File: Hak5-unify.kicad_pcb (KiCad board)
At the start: 2 copper layers, 26 x 17.5 mm, 4 parts, among them J1 Conn_01x04, J2 Conn_01x03, U1 Unify-Nano

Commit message: v0.1.1
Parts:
- removed 10K: R, Resistors_ThroughHole:R_Axial_DIN0204_L3.6mm_D1.6mm_P7.62mm_Horizontal
- added R1: R, Resistors_ThroughHole:R_Axial_DIN0204_L3.6mm_D1.6mm_P7.62mm_Horizontal, F.Cu at (104.0, 86.5)
- moved J1 1.00 mm to (123.2, 93.6)
- moved U1 0.63 mm to (106.1, 97.8)
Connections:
- J2 pad 1: Net-(J2-Pad1) -> +5V
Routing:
- net TX: track 35.3 -> 36.8 mm
- net +5V: track 5.03 -> 4.47 mm
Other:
- outline, holes or cut-outs redrawn
- board text added: "Cut Out"
- board text added: "v0.1.1"
- board text removed: "v0.1.0"

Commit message: v0.2.0
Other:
- outline, holes or cut-outs redrawn
- board text added: "v0.2.0"
- board text removed: "v0.1.1"
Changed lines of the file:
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@@
   (general
     (thickness 1.6)
-    (drawings 19)
+    (drawings 23)
     (tracks 17)
     (zones 0)
@@
     (uvia_drill 0.1)
   )
+  (module unify-nano:unify-nano (layer F.Cu)
+    (at 106.1 97.75)
+    (fp_text reference U1 (at 0.3 3.5) (layer F.SilkS)
+      (effects (font (size 1 1) (thickness 0.15)))
+    )
+    (fp_text value Unify-Nano (at 7 1) (layer F.Fab)
+      (effects (font (size 1 1) (thickness 0.15)))
+    )
+    (fp_line (start 0 0) (end 0 -13.1) (layer F.Fab) (width 0.15))
+    (fp_line (start 14.6 -13.1) (end 0 -13.1) (layer F.Fab) (width 0.15))
+    (fp_line (start 14.6 0) (end 14.6 -13.1) (layer F.Fab) (width 0.15))
+    (fp_line (start 0 0) (end 14.6 0) (layer F.Fab) (width 0.15))
+    (pad 9 thru_hole circle (at 12.2 -13.3) (size 1.524 1.524) (drill 0.762) (layers *.Cu *.Mask)
+      (net 9 "Net-(SW1-Pad2)"))
+    (pad 10 thru_hole circle (at 8.6 -13.3) (size 1.524 1.524) (drill 0.762) (layers *.Cu *.Mask)
+      (net 10 "Net-(SW1-Pad1)"))
+    (pad 8 thru_hole circle (at 14.8 -5) (size 1.524 1.524) (drill 0.762) (layers *.Cu *.Mask)
+      (net 11 "Net-(U1-Pad8)"))
+    (pad 7 thru_hole circle (at 14.7 -1.8) (size 1.524 1.524) (drill 0.762) (layers *.Cu *.Mask)
+      (net 12 "Net-(U1-Pad7)"))
+    (pad 6 thru_hole circle (at -0.25 -1.5) (size 1.524 1.524) (drill 0.762) (layers *.Cu *.Mask)
+      (net 2 +5V))
+    (pad 5 thru_hole circle (at -0.25 -3.5) (size 1.524 1.524) (drill 0.762) (layers *.Cu *.Mask)
+      (net 1 GND))
+    (pad 4 thru_hole circle (at -0.25 -5.5) (size 1.524 1.524) (drill 0.762) (layers *.Cu *.Mask)
+      (net 4 "Net-(U1-Pad4)"))
+    (pad 3 thru_hole circle (at -0.25 -7.5) (size 1.524 1.524) (drill 0.762) (layers *.Cu *.Mask)
+      (net 3 "Net-(U1-Pad3)"))
+    (pad 2 thru_hole circle (at -0.25 -9.5) (size 1.524 1.524) (drill 0.762) (layers *.Cu *.Mask)
+      (net 13 "Net-(J2-Pad3)"))
+    (pad 1 thru_hole circle (at -0.25 -11.5) (size 1.524 1.524) (drill 0.762) (layers *.Cu *.Mask)
+      (net 6 TX))
+  )
   (module Pin_Headers:Pin_Header_Straight_1x03_Pitch2.54mm (layer F.Cu)
     (at 101.6 96.2 180)
@@
       (rotate (xyz 0 0 0))
     )
-  )
-  (module unify-nano:unify-nano (layer F.Cu)
-    (at 106.1 97.8)
-    (fp_text reference U1 (at 0.3 3.5) (layer F.SilkS)
-      (effects (font (size 1 1) (thickness 0.15)))
-    )
-    (fp_text value Unify-Nano (at 7 1) (layer F.Fab)
-      (effects (font (size 1 1) (thickness 0.15)))
-    )
-    (fp_line (start 0 0) (end 0 -13.2) (layer F.Fab) (width 0.15))
-    (fp_line (start 14.65 -13.2) (end -0.05 -13.2) (layer F.Fab) (width 0.15))
-    (fp_line (start 14.65 0) (end 14.65 -13.2) (layer F.Fab) (width 0.15))
-    (fp_line (start 0.05 0) (end 14.65 0) (layer F.Fab) (width 0.15))
-    (pad 9 thru_hole circle (at 12.2 -13.4) (size 1.524 1.524) (drill 0.762) (layers *.Cu *.Mask)
-      (net 9 "Net-(SW1-Pad2)"))
-    (pad 10 thru_hole circle (at 8.65 -13.4) (size 1.524 1.524) (drill 0.762) (layers *.Cu *.Mask)
-      (net 10 "Net-(SW1-Pad1)"))
-    (pad 8 thru_hole circle (at 14.85 -5) (size 1.524 1.524) (drill 0.762) (layers *.Cu *.Mask)
-      (net 11 "Net-(U1-Pad8)"))
-    (pad 7 thru_hole circle (at 14.9 -1.75) (size 1.524 1.524) (drill 0.762) (layers *.Cu *.Mask)
-      (net 12 "Net-(U1-Pad7)"))
-    (pad 6 thru_hole circle (at -0.25 -1.5) (size 1.524 1.524) (drill 0.762) (layers *.Cu *.Mask)
-      (net 2 +5V))
-    (pad 5 thru_hole circle (at -0.25 -3.5) (size 1.524 1.524) (drill 0.762) (layers *.Cu *.Mask)
-      (net 1 GND))
-    (pad 4 thru_hole circle (at -0.25 -5.5) (size 1.524 1.524) (drill 0.762) (layers *.Cu *.Mask)
-      (net 4 "Net-(U1-Pad4)"))
-    (pad 3 thru_hole circle (at -0.25 -7.5) (size 1.524 1.524) (drill 0.762) (layers *.Cu *.Mask)
-      (net 3 "Net-(U1-Pad3)"))
-    (pad 2 thru_hole circle (at -0.25 -9.5) (size 1.524 1.524) (drill 0.762) (layers *.Cu *.Mask)
-      (net 13 "Net-(J2-Pad3)"))
-    (pad 1 thru_hole circle (at -0.25 -11.5) (size 1.524 1.524) (drill 0.762) (layers *.Cu *.Mask)
-      (net 6 TX))
   )
   (module Resistors_ThroughHole:R_Axial_DIN0204_L3.6mm_D1.6mm_P7.62mm_Horizontal (layer F.Cu)
@@
     )
   )
+  (gr_circle (center 106 84.6) (end 106.25 84.6) (layer Edge.Cuts) (width 0.2))
+  (gr_circle (center 106 97.9) (end 106.25 97.9) (layer Edge.Cuts) (width 0.2))
+  (gr_circle (center 120.8 97.9) (end 121.05 97.9) (layer Edge.Cuts) (width 0.2))
+  (gr_circle (center 120.7 84.6) (end 120.95 84.6) (layer Edge.Cuts) (width 0.2))
   (gr_line (start 124.4 82.5) (end 126 84.1) (layer Edge.Cuts) (width 0.2))
   (gr_line (start 100 84.5) (end 101.9 82.5) (layer Edge.Cuts) (width 0.2))
@@
     (effects (font (size 0.65 0.65) (thickness 0.1625)))
   )
-  (gr_text v0.1.1 (at 102.6 85.8 45) (layer F.SilkS)
-    (effects (font (size 0.5 0.5) (thickness 0.125)))
-  )
-  (gr_text "HawkVision\n" (at 102.3 84.8 45) (layer F.SilkS)
-    (effects (font (size 0.65 0.65) (thickness 0.125)))
+  (gr_text v0.2.0 (at 102.7 85.9 45) (layer F.SilkS)
+    (effects (font (size 0.7 0.7) (thickness 0.125)))
+  )
+  (gr_text "HawkVision\n" (at 102.4 84.8 45) (layer F.SilkS)
+    (effects (font (size 0.7 0.7) (thickness 0.125)))
   )
   (gr_line (start 101.9 82.5) (end 124.4 82.5) (layer Edge.Cuts) (width 0.2))
-  (gr_line (start 106 98) (end 121 98) (layer Edge.Cuts) (width 0.2))
-  (gr_line (start 105.9 84.3) (end 105.9 97.9) (layer Edge.Cuts) (width 0.2))
-  (gr_line (start 120.9 84.3) (end 105.9 84.3) (layer Edge.Cuts) (width 0.2))
-  (gr_line (start 121 97.9) (end 121 84.4) (layer Edge.Cuts) (width 0.2))
+  (gr_line (start 106 97.9) (end 120.9 97.9) (layer Edge.Cuts) (width 0.2))
+  (gr_line (start 106 84.5) (end 106 97.8) (layer Edge.Cuts) (width 0.2))
+  (gr_line (start 120.9 84.6) (end 105.9 84.6) (layer Edge.Cuts) (width 0.2))
+  (gr_line (start 120.8 97.8) (end 120.8 84.5) (layer Edge.Cuts) (width 0.2))
   (segment (start 103.82 93.66) (end 104.14 93.98) (width 0.5) (layer F.Cu) (net 1))
   (segment (start 101.6 93.66) (end 103.82 93.66) (width 0.5) (layer F.Cu) (net 1))

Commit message: plot 0.2.1
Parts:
- added J1: Conn_01x04, Pin_Headers:Pin_Header_Straight_1x04_Pitch2.54mm, F.Cu at (183.2, 32.0)
- added J1: Conn_01x04, Pin_Headers:Pin_Header_Straight_1x04_Pitch2.54mm, F.Cu at (183.2, 93.6)
- added J1: Conn_01x04, Pin_Headers:Pin_Header_Straight_1x04_Pitch2.54mm, F.Cu at (153.2, 93.6)
- added J1: Conn_01x04, Pin_Headers:Pin_Header_Straight_1x04_Pitch2.54mm, F.Cu at (153.2, 32.0)
- added J1: Conn_01x04, Pin_Headers:Pin_Header_Straight_1x04_Pitch2.54mm, F.Cu at (123.2, 32.0)
- added J1: Conn_01x04, Pin_Headers:Pin_Header_Straight_1x04_Pitch2.54mm, F.Cu at (183.2, 52.5)
- added J1: Conn_01x04, Pin_Headers:Pin_Header_Straight_1x04_Pitch2.54mm, F.Cu at (153.2, 52.5)
- added J1: Conn_01x04, Pin_Headers:Pin_Header_Straight_1x04_Pitch2.54mm, F.Cu at (123.2, 52.5)
- added J1: Conn_01x04, Pin_Headers:Pin_Header_Straight_1x04_Pitch2.54mm, F.Cu at (183.2, 73.1)
- added J1: Conn_01x04, Pin_Headers:Pin_Header_Straight_1x04_Pitch2.54mm, F.Cu at (153.2, 73.1)
- added J1: Conn_01x04, Pin_Headers:Pin_Header_Straight_1x04_Pitch2.54mm, F.Cu at (123.2, 73.1)
- added J2: Conn_01x03, Pin_Headers:Pin_Header_Straight_1x03_Pitch2.54mm, F.Cu at (161.6, 34.6)
- added J2: Conn_01x03, Pin_Headers:Pin_Header_Straight_1x03_Pitch2.54mm, F.Cu at (161.6, 96.2)
- added J2: Conn_01x03, Pin_Headers:Pin_Header_Straight_1x03_Pitch2.54mm, F.Cu at (131.6, 96.2)
- added J2: Conn_01x03, Pin_Headers:Pin_Header_Straight_1x03_Pitch2.54mm, F.Cu at (131.6, 34.6)
- added J2: Conn_01x03, Pin_Headers:Pin_Header_Straight_1x03_Pitch2.54mm, F.Cu at (101.6, 34.6)
- added J2: Conn_01x03, Pin_Headers:Pin_Header_Straight_1x03_Pitch2.54mm, F.Cu at (161.6, 55.1)
- added J2: Conn_01x03, Pin_Headers:Pin_Header_Straight_1x03_Pitch2.54mm, F.Cu at (131.6, 55.1)
- added J2: Conn_01x03, Pin_Headers:Pin_Header_Straight_1x03_Pitch2.54mm, F.Cu at (101.6, 55.1)
- added J2: Conn_01x03, Pin_Headers:Pin_Header_Straight_1x03_Pitch2.54mm, F.Cu at (161.6, 75.7)
- added J2: Conn_01x03, Pin_Headers:Pin_Header_Straight_1x03_Pitch2.54mm, F.Cu at (131.6, 75.7)
- added J2: Conn_01x03, Pin_Headers:Pin_Header_Straight_1x03_Pitch2.54mm, F.Cu at (101.6, 75.7)
- added R1: R, Resistors_ThroughHole:R_Axial_DIN0204_L3.6mm_D1.6mm_P7.62mm_Horizontal, F.Cu at (164.0, 24.9)
- added R1: R, Resistors_ThroughHole:R_Axial_DIN0204_L3.6mm_D1.6mm_P7.62mm_Horizontal, F.Cu at (164.0, 86.5)
- added R1: R, Resistors_ThroughHole:R_Axial_DIN0204_L3.6mm_D1.6mm_P7.62mm_Horizontal, F.Cu at (134.0, 86.5)
- added R1: R, Resistors_ThroughHole:R_Axial_DIN0204_L3.6mm_D1.6mm_P7.62mm_Horizontal, F.Cu at (134.0, 24.9)
- added R1: R, Resistors_ThroughHole:R_Axial_DIN0204_L3.6mm_D1.6mm_P7.62mm_Horizontal, F.Cu at (104.0, 24.9)
- added R1: R, Resistors_ThroughHole:R_Axial_DIN0204_L3.6mm_D1.6mm_P7.62mm_Horizontal, F.Cu at (164.0, 45.4)
- added R1: R, Resistors_ThroughHole:R_Axial_DIN0204_L3.6mm_D1.6mm_P7.62mm_Horizontal, F.Cu at (134.0, 45.4)
- added R1: R, Resistors_ThroughHole:R_Axial_DIN0204_L3.6mm_D1.6mm_P7.62mm_Horizontal, F.Cu at (104.0, 45.4)
- added R1: R, Resistors_ThroughHole:R_Axial_DIN0204_L3.6mm_D1.6mm_P7.62mm_Horizontal, F.Cu at (164.0, 66.0)
- added R1: R, Resistors_ThroughHole:R_Axial_DIN0204_L3.6mm_D1.6mm_P7.62mm_Horizontal, F.Cu at (134.0, 66.0)
- added R1: R, Resistors_ThroughHole:R_Axial_DIN0204_L3.6mm_D1.6mm_P7.62mm_Horizontal, F.Cu at (104.0, 66.0)
- added U1: Unify-Nano, unify-nano:unify-nano, F.Cu at (166.1, 36.1)
- added U1: Unify-Nano, unify-nano:unify-nano, F.Cu at (166.1, 97.8)
- added U1: Unify-Nano, unify-nano:unify-nano, F.Cu at (136.1, 97.8)
- added U1: Unify-Nano, unify-nano:unify-nano, F.Cu at (136.1, 36.1)
- added U1: Unify-Nano, unify-nano:unify-nano, F.Cu at (106.1, 36.1)
- added U1: Unify-Nano, unify-nano:unify-nano, F.Cu at (166.1, 56.7)
- added U1: Unify-Nano, unify-nano:unify-nano, F.Cu at (136.1, 56.7)
- added U1: Unify-Nano, unify-nano:unify-nano, F.Cu at (106.1, 56.7)
- added U1: Unify-Nano, unify-nano:unify-nano, F.Cu at (166.1, 77.2)
- added U1: Unify-Nano, unify-nano:unify-nano, F.Cu at (136.1, 77.2)
- added U1: Unify-Nano, unify-nano:unify-nano, F.Cu at (106.1, 77.2)
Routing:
- net TX: track 36.8 -> 441.7 mm
- net Net-(J2-Pad3): track 5.42 -> 65.1 mm
- net GND: track 4.77 -> 57.3 mm
- net +5V: track 4.47 -> 53.7 mm
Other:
- board size 26 x 17.5 mm -> 96.1 x 90 mm
- board text added: "Designed by Spencer in Utah"
- board text added: "v0.2.1"
- board text removed: "v0.2.0"

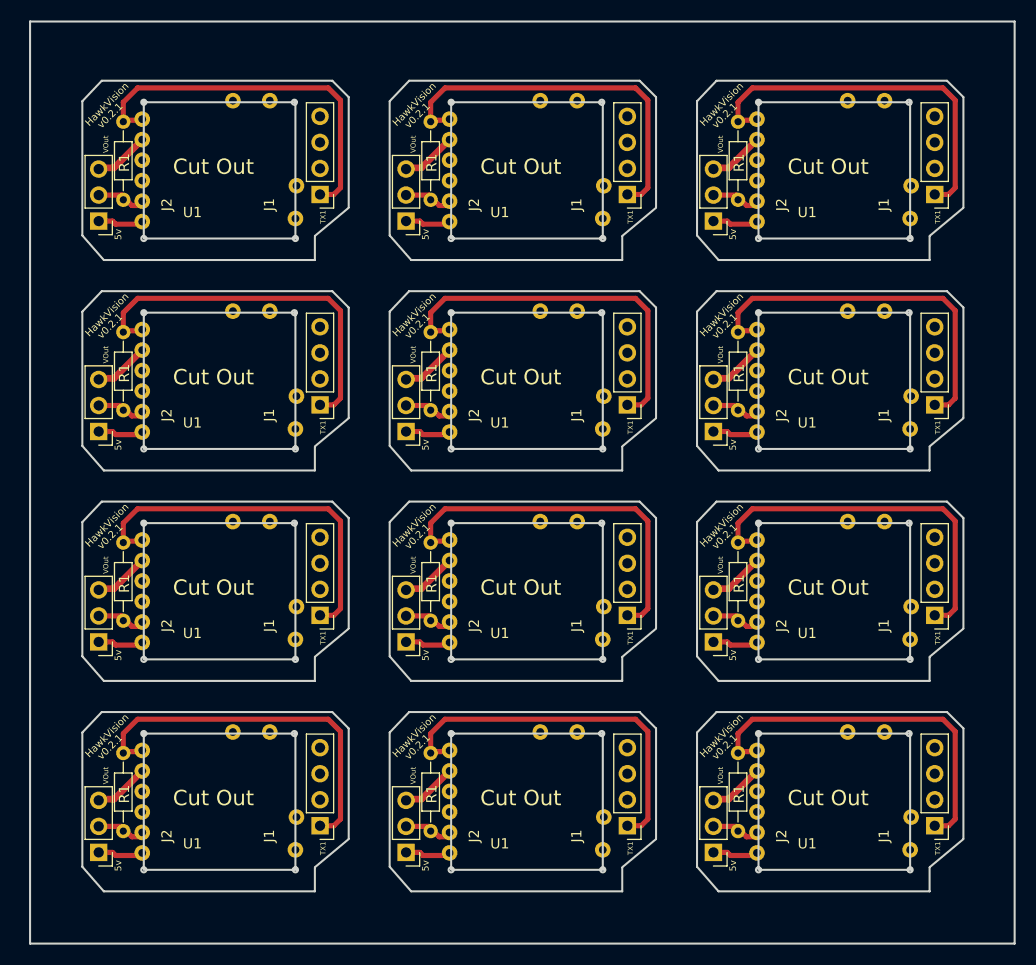
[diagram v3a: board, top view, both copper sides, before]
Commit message: no panelization
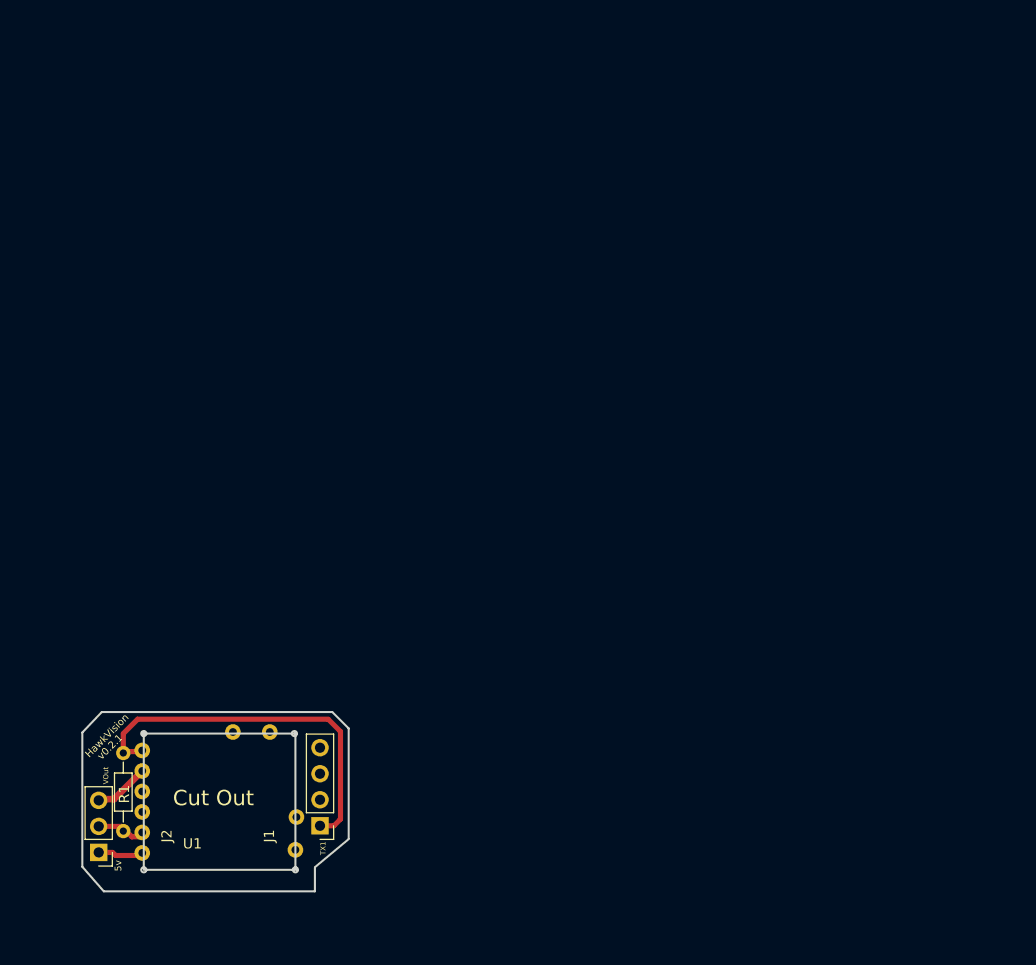
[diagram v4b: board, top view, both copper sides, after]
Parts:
- removed the J1 at (183.2, 32.0)
- removed the J1 at (183.2, 93.6)
- removed the J1 at (153.2, 93.6)
- removed the J1 at (153.2, 32.0)
- removed the J1 at (123.2, 32.0)
- removed the J1 at (183.2, 52.5)
- removed the J1 at (153.2, 52.5)
- removed the J1 at (123.2, 52.5)
- removed the J1 at (183.2, 73.1)
- removed the J1 at (153.2, 73.1)
- removed the J1 at (123.2, 73.1)
- removed the J2 at (161.6, 34.6)
- removed the J2 at (161.6, 96.2)
- removed the J2 at (131.6, 96.2)
- removed the J2 at (131.6, 34.6)
- removed the J2 at (101.6, 34.6)
- removed the J2 at (161.6, 55.1)
- removed the J2 at (131.6, 55.1)
- removed the J2 at (101.6, 55.1)
- removed the J2 at (161.6, 75.7)
- removed the J2 at (131.6, 75.7)
- removed the J2 at (101.6, 75.7)
- removed the R1 at (164.0, 24.9)
- removed the R1 at (164.0, 86.5)
- removed the R1 at (134.0, 86.5)
- removed the R1 at (134.0, 24.9)
- removed the R1 at (104.0, 24.9)
- removed the R1 at (164.0, 45.4)
- removed the R1 at (134.0, 45.4)
- removed the R1 at (104.0, 45.4)
- removed the R1 at (164.0, 66.0)
- removed the R1 at (134.0, 66.0)
- removed the R1 at (104.0, 66.0)
- removed the U1 at (166.1, 36.1)
- removed the U1 at (166.1, 97.8)
- removed the U1 at (136.1, 97.8)
- removed the U1 at (136.1, 36.1)
- removed the U1 at (106.1, 36.1)
- removed the U1 at (166.1, 56.7)
- removed the U1 at (136.1, 56.7)
- removed the U1 at (106.1, 56.7)
- removed the U1 at (166.1, 77.2)
- removed the U1 at (136.1, 77.2)
- removed the U1 at (106.1, 77.2)
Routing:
- net TX: track 441.7 -> 36.8 mm
- net Net-(J2-Pad3): track 65.1 -> 5.42 mm
- net GND: track 57.3 -> 4.77 mm
- net +5V: track 53.7 -> 4.47 mm
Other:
- board size 96.1 x 90 mm -> 26 x 17.5 mm

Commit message: v0.3.0
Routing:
- net TX: track 36.8 -> 32.4 mm
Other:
- board size 26 x 17.5 mm -> 24.8 x 17.5 mm
- board text added: "v0.3.0"
- board text removed: "v0.2.1"
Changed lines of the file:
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@@
   (general
     (thickness 1.6)
-    (drawings 24)
+    (drawings 21)
     (tracks 17)
     (zones 0)
@@
   )
   (setup
-    (last_trace_width 0.25)
+    (last_trace_width 0.5)
     (user_trace_width 0.5)
     (user_trace_width 0.65)
@@
     (mod_text_size 1 1)
     (mod_text_width 0.15)
-    (pad_size 1.524 1.524)
-    (pad_drill 0.762)
+    (pad_size 2.2 2.2)
+    (pad_drill 1.5)
     (pad_to_mask_clearance 0.2)
     (aux_axis_origin 0 0)
@@
     )
   )
+  (gr_line (start 123 98) (end 121.1 100) (layer Edge.Cuts) (width 0.2))
   (gr_text "Designed by Spencer in Utah" (at 113.45 98.95) (layer B.SilkS)
     (effects (font (size 0.65 0.65) (thickness 0.1625)) (justify mirror))
   )
-  (gr_circle (center 106 84.6) (end 106.25 84.6) (layer Edge.Cuts) (width 0.2))
-  (gr_circle (center 106 97.9) (end 106.25 97.9) (layer Edge.Cuts) (width 0.2))
-  (gr_circle (center 120.8 97.9) (end 121.05 97.9) (layer Edge.Cuts) (width 0.2))
-  (gr_circle (center 120.7 84.6) (end 120.95 84.6) (layer Edge.Cuts) (width 0.2))
-  (gr_line (start 124.4 82.5) (end 126 84.1) (layer Edge.Cuts) (width 0.2))
+  (gr_line (start 123.2 82.5) (end 124.8 84.1) (layer Edge.Cuts) (width 0.2))
   (gr_line (start 100 84.5) (end 101.9 82.5) (layer Edge.Cuts) (width 0.2))
   (gr_line (start 100 97.6) (end 102.1 100) (layer Edge.Cuts) (width 0.2))
-  (gr_line (start 122.7 97.7) (end 122.7 100) (layer Edge.Cuts) (width 0.2))
-  (gr_line (start 126 94.9) (end 122.7 97.65) (layer Edge.Cuts) (width 0.2))
+  (gr_line (start 123 95.5) (end 123 98) (layer Edge.Cuts) (width 0.2))
+  (gr_line (start 124.8 95.4) (end 123 95.4) (layer Edge.Cuts) (width 0.2))
   (gr_text "Cut Out" (at 112.8 90.9) (layer F.SilkS)
     (effects (font (size 1.5 1.5) (thickness 0.3)))
   )
-  (gr_line (start 126 84.1) (end 126 94.85) (layer Edge.Cuts) (width 0.2))
+  (gr_line (start 124.8 84.2) (end 124.8 95.3) (layer Edge.Cuts) (width 0.2))
   (gr_line (start 100 84.5) (end 100 97.6) (layer Edge.Cuts) (width 0.2))
-  (gr_line (start 102.1 100) (end 122.7 100) (layer Edge.Cuts) (width 0.2))
-  (gr_text TX1 (at 123.5 95.8 90) (layer F.SilkS)
+  (gr_line (start 102.1 100) (end 121.1 100) (layer Edge.Cuts) (width 0.2))
+  (gr_text TX1 (at 122.4 95.4 90) (layer F.SilkS)
     (effects (font (size 0.5 0.5) (thickness 0.125)))
   )
@@
     (effects (font (size 0.65 0.65) (thickness 0.1625)))
   )
-  (gr_text v0.2.1 (at 102.7 85.9 45) (layer F.SilkS)
+  (gr_text v0.3.0 (at 102.7 85.9 45) (layer F.SilkS)
     (effects (font (size 0.7 0.7) (thickness 0.125)))
   )
@@
     (effects (font (size 0.7 0.7) (thickness 0.125)))
   )
-  (gr_line (start 101.9 82.5) (end 124.4 82.5) (layer Edge.Cuts) (width 0.2))
-  (gr_line (start 106 97.9) (end 120.9 97.9) (layer Edge.Cuts) (width 0.2))
-  (gr_line (start 106 84.5) (end 106 97.8) (layer Edge.Cuts) (width 0.2))
-  (gr_line (start 120.9 84.6) (end 105.9 84.6) (layer Edge.Cuts) (width 0.2))
-  (gr_line (start 120.8 97.8) (end 120.8 84.5) (layer Edge.Cuts) (width 0.2))
+  (gr_line (start 101.9 82.5) (end 123.2 82.5) (layer Edge.Cuts) (width 0.2))
+  (gr_line (start 106 98) (end 120.8 98) (layer Edge.Cuts) (width 0.2))
+  (gr_line (start 106 84.6) (end 106 97.9) (layer Edge.Cuts) (width 0.2))
+  (gr_line (start 120.8 84.6) (end 106 84.6) (layer Edge.Cuts) (width 0.2))
+  (gr_line (start 120.8 97.9) (end 120.8 84.6) (layer Edge.Cuts) (width 0.2))
   (segment (start 103.82 93.66) (end 104.14 93.98) (width 0.5) (layer F.Cu) (net 1))
   (segment (start 101.6 93.66) (end 103.82 93.66) (width 0.5) (layer F.Cu) (net 1))
@@
   (segment (start 101.6 96.2) (end 102.95 96.2) (width 0.5) (layer F.Cu) (net 2))
   (segment (start 104.14 86.36) (end 105.94999 86.36) (width 0.5) (layer F.Cu) (net 6))
-  (segment (start 124.55 93.6) (end 125.2 92.95) (width 0.5) (layer F.Cu) (net 6))
-  (segment (start 123.2 93.6) (end 124.55 93.6) (width 0.5) (layer F.Cu) (net 6))
-  (segment (start 125.2 92.95) (end 125.2 84.4) (width 0.5) (layer F.Cu) (net 6))
-  (segment (start 125.2 84.4) (end 124 83.2) (width 0.5) (layer F.Cu) (net 6))
-  (segment (start 124 83.2) (end 105.4 83.2) (width 0.5) (layer F.Cu) (net 6))
-  (segment (start 104 84.6) (end 104 86.5) (width 0.5) (layer F.Cu) (net 6))
-  (segment (start 105.4 83.2) (end 104 84.6) (width 0.5) (layer F.Cu) (net 6))
+  (segment (start 123.2 93.256238) (end 123.2 93.6) (width 0.5) (layer F.Cu) (net 6))
+  (segment (start 121.7 91.756238) (end 123.2 93.256238) (width 0.5) (layer F.Cu) (net 6))
+  (segment (start 120.7 83.2) (end 121.7 84.2) (width 0.5) (layer F.Cu) (net 6))
+  (segment (start 121.7 84.2) (end 121.7 91.756238) (width 0.5) (layer F.Cu) (net 6))
+  (segment (start 104 84.6) (end 105.4 83.2) (width 0.5) (layer F.Cu) (net 6))
+  (segment (start 105.4 83.2) (end 120.7 83.2) (width 0.5) (layer F.Cu) (net 6))
+  (segment (start 104 86.5) (end 104 84.6) (width 0.5) (layer F.Cu) (net 6))
   (segment (start 103.1 91) (end 105.87499 88.22501) (width 0.65) (layer F.Cu) (net 13))
   (segment (start 101.6 91) (end 103.1 91) (width 0.65) (layer F.Cu) (net 13))

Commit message: 2holes
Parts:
- J1: value Conn_01x04 -> Conn_01x02; footprint Pin_Headers:Pin_Header_Straight_1x04_Pitch2.54mm -> Pin_Headers:Pin_Header_Straight_1x02_Pitch2.54mm
- moved J1 2.54 mm to (125.7, 93.5)
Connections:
- net RX renamed Net-(J1-Pad2)
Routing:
- net TX: track 32.4 -> 33.1 mm
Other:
- board size 24.8 x 17.5 mm -> 27.3 x 17.5 mm
